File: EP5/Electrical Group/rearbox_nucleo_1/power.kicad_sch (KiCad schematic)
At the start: 10 parts, among them IC1 LMQ66420MC5RXBRQ1, J6 power board

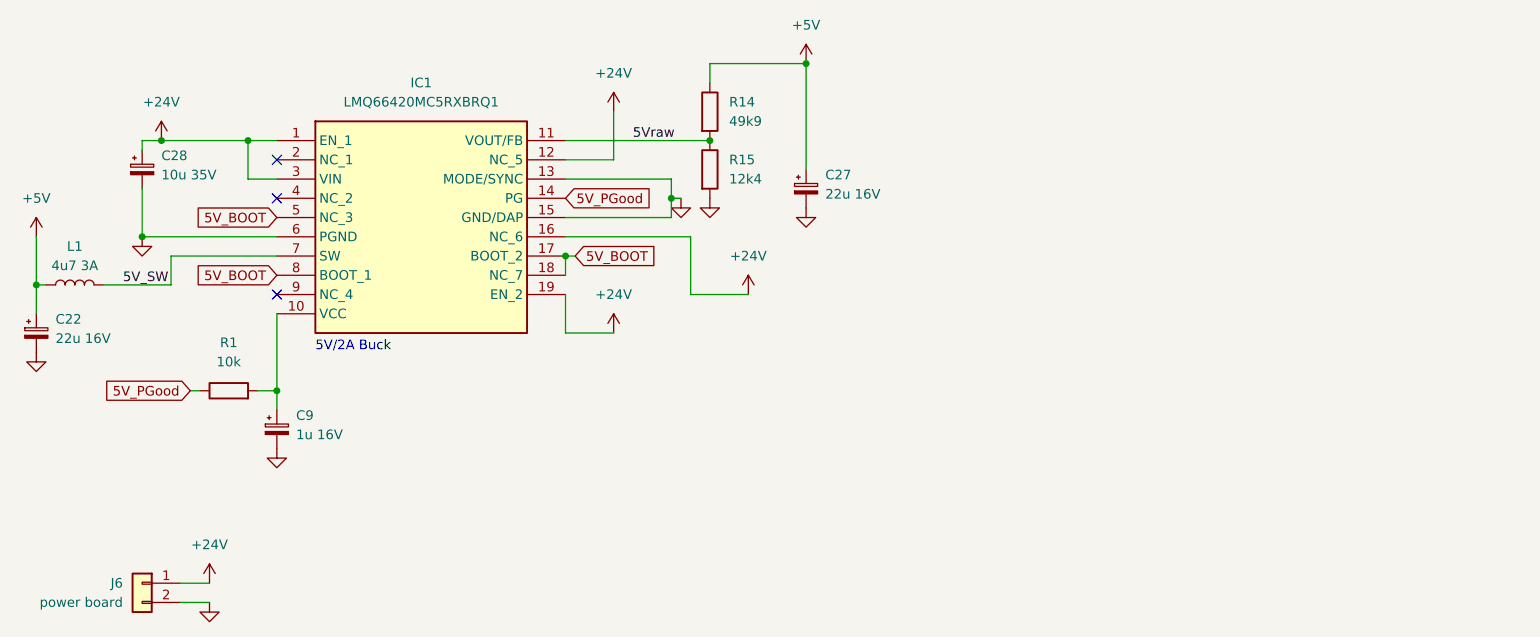
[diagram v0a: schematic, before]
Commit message: update rearbox Nucleo hat to V2.0 to cancel isolation and use IDC socket
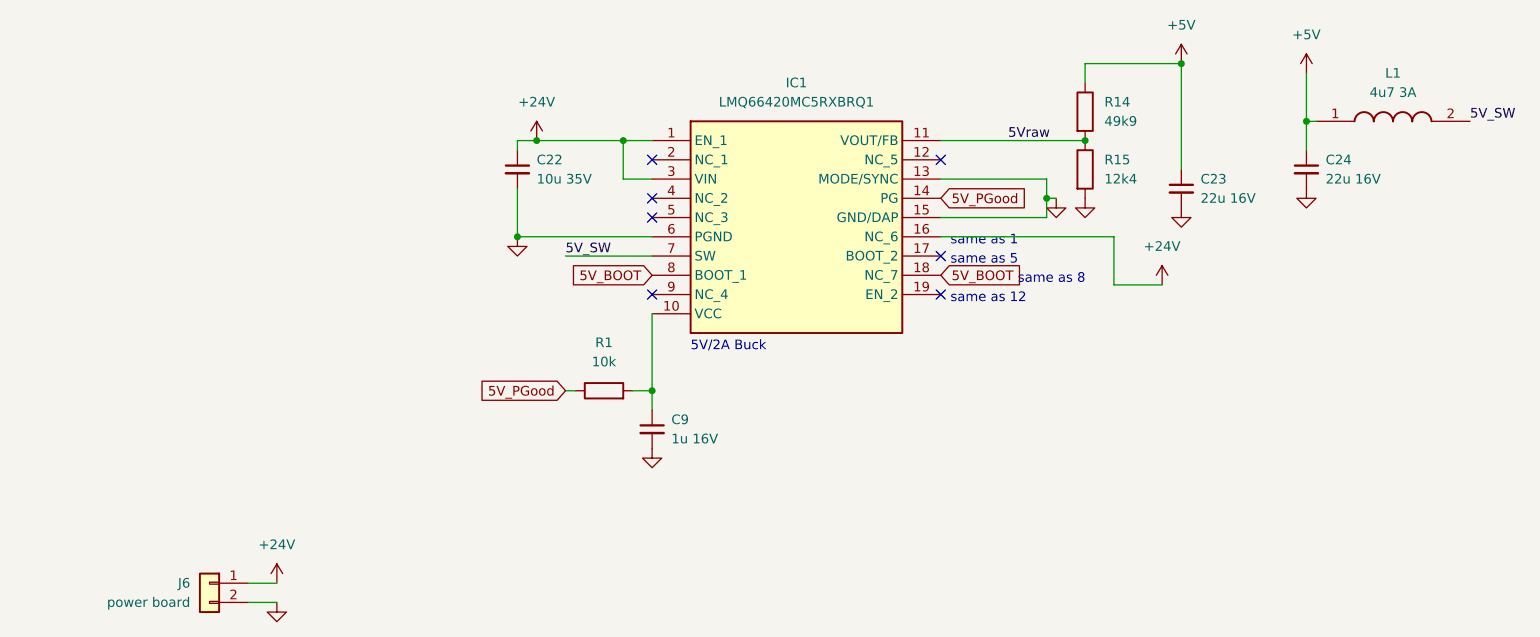
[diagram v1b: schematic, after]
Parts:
- removed C22, C27: 22u 16V, Capacitor_THT:CP_Radial_D5.0mm_P2.50mm, symbol Device:C_Polarized_Small
- removed C28: 10u 35V, Capacitor_THT:CP_Radial_D5.0mm_P2.50mm, symbol Device:C_Polarized_Small
- removed C9: 1u 16V, Capacitor_SMD:C_0805_2012Metric, symbol Device:C_Polarized_Small
- removed L1: 4u7 3A, Inductor_SMD:L_0805_2012Metric, symbol Device:L
- added C22: 10u 35V, Capacitor_SMD:C_1206_3216Metric, symbol Device:C_Small
- added C23, C24: 22u 16V, Capacitor_SMD:C_1206_3216Metric, symbol Device:C_Small
- added C9: 1u 16V, Capacitor_SMD:C_0805_2012Metric, symbol Device:C_Small
- added L1: 4u7 3A, SamacSys_Parts:INDPM5552X300N, symbol SamacSys_Parts:SRP5030WA-2R2M
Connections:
- net +24V: now also C22.1; no longer IC1.12 (NC_5), IC1.19 (EN_2)
- net +5V: now also C23.1, C24.1, L1.1
- net 5V_BOOT: no longer IC1.17 (BOOT_2), IC1.5 (NC_3)
- net 5V_SW: now also L1.2
- net GND: now also C22.2, C23.2, C24.2, C9.2
- net at IC1.10 (VCC), R1.2: now also C9.1
- no-connect marks 3 -> 7
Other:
- note added: "same as 1"
- note added: "same as 12"
- note added: "same as 5"
- note added: "same as 8"
- company: (none) -> NTURacing
- title: (none) -> rear box nucleo board 1
- moved on the sheet: J6, R1, R14, R15

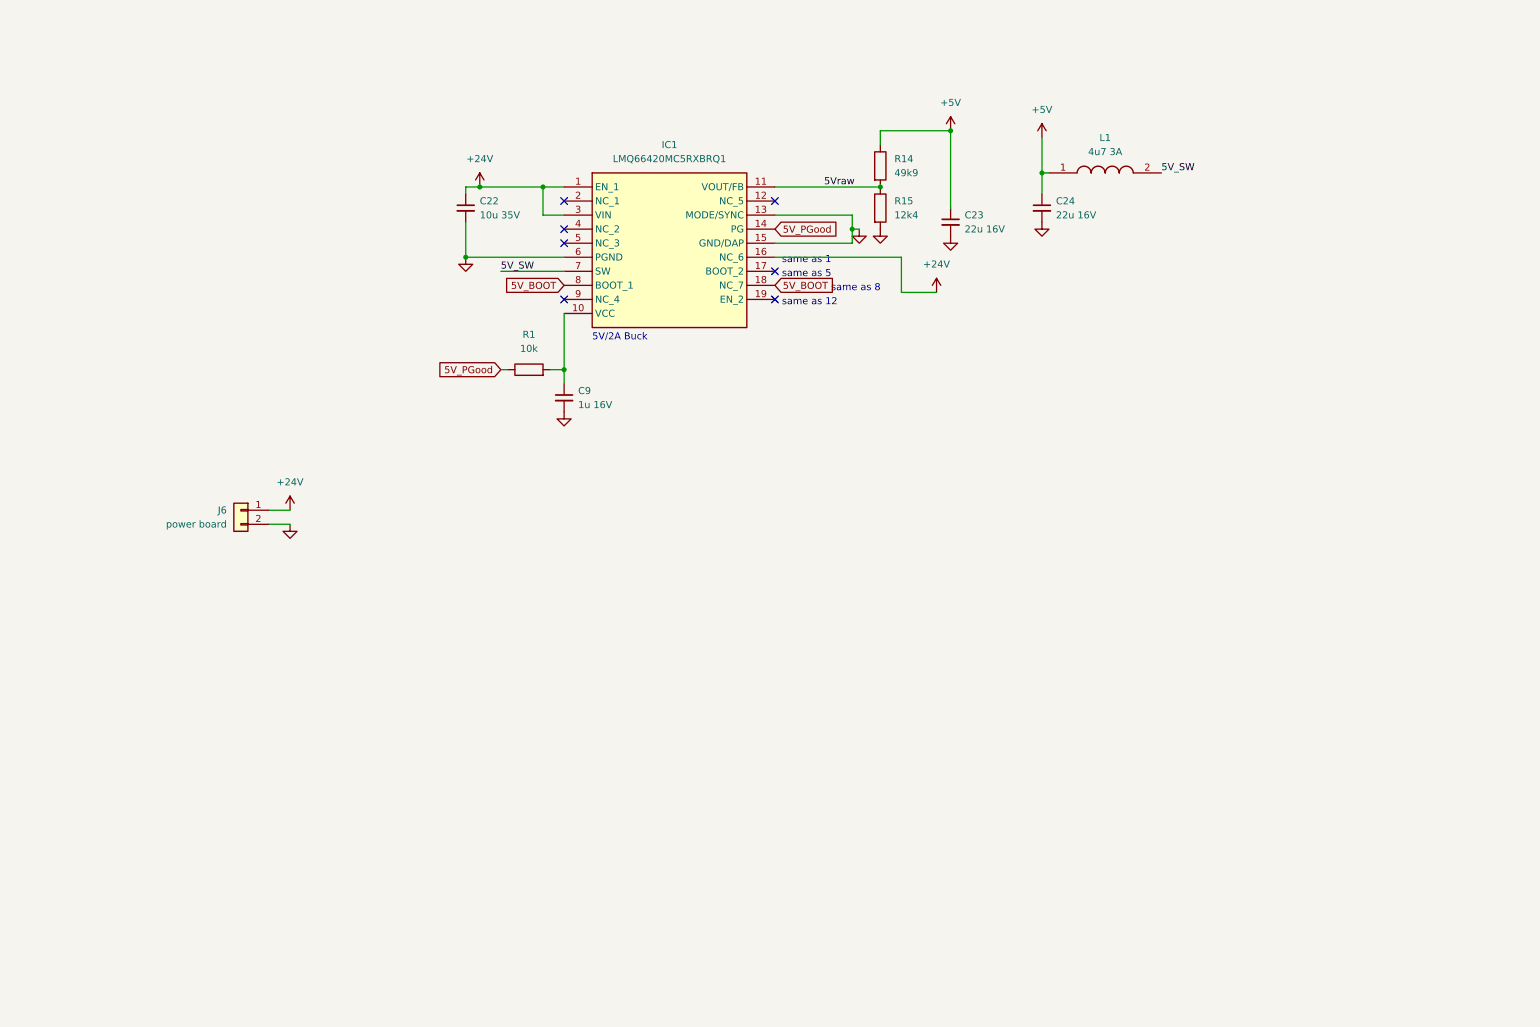
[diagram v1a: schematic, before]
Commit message: update rearbox nucleo hat to V3.0
change buck converter
add fuses and Zener diodes
change CAN transceiver
change power supply of brake light
change MOSFET for buzzer and brake light control
add test pads
add LEDs
fix SD card pin
fix VBAT reveresed
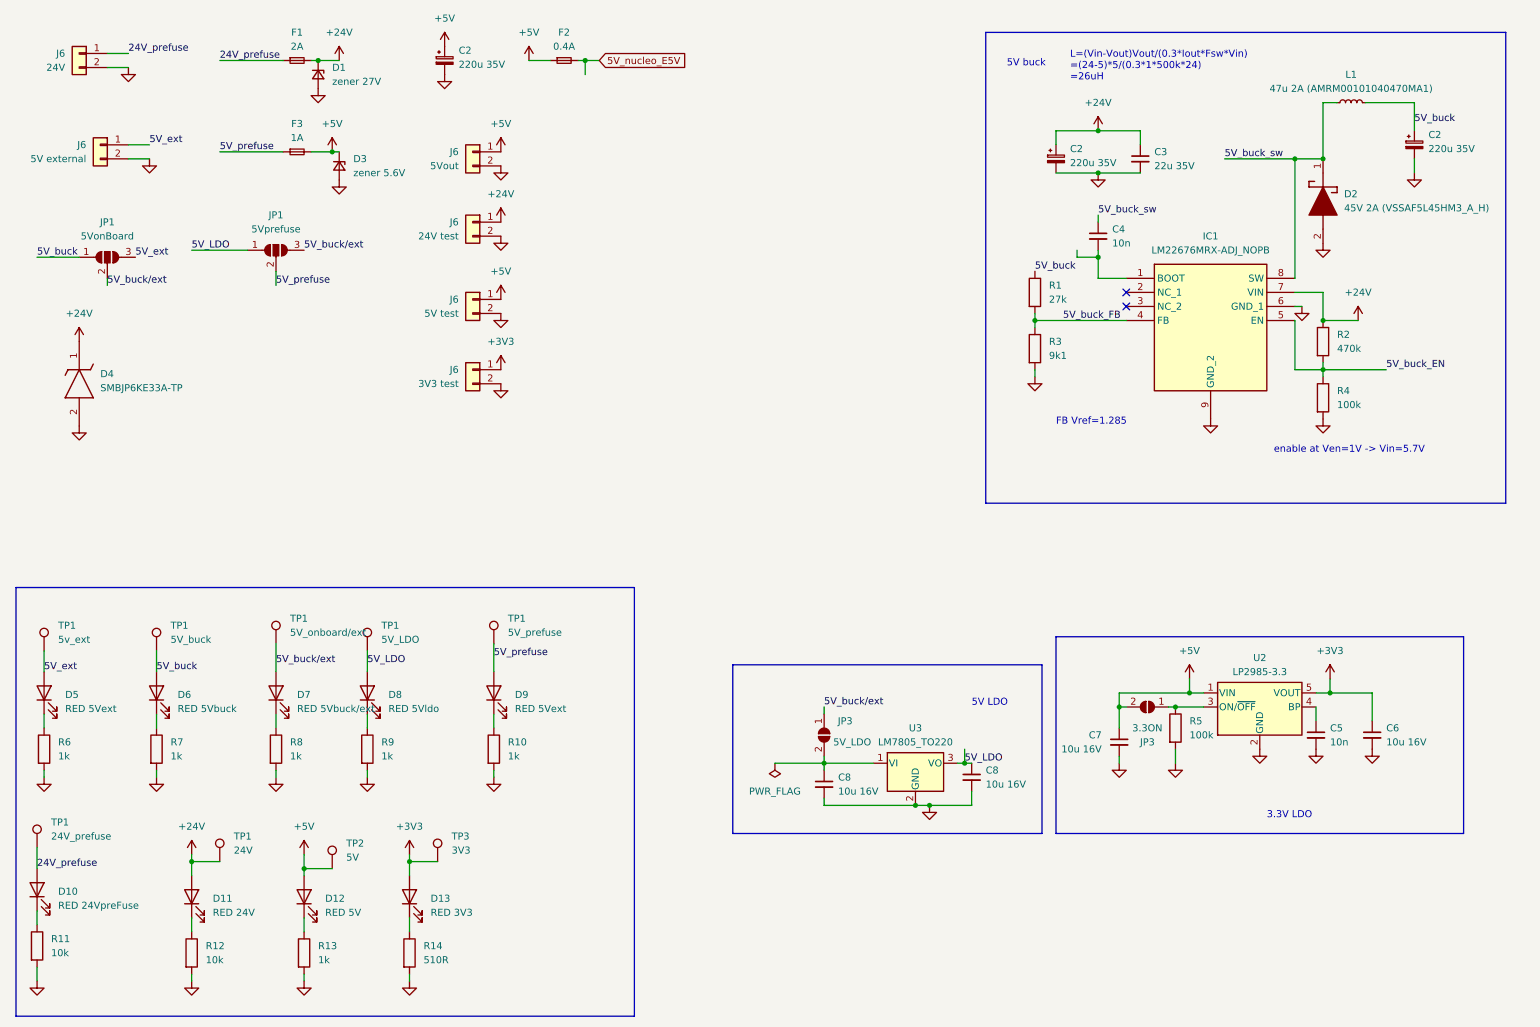
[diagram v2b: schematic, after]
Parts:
- removed C22: 10u 35V, Capacitor_SMD:C_1206_3216Metric, symbol Device:C_Small
- removed C23, C24: 22u 16V, Capacitor_SMD:C_1206_3216Metric, symbol Device:C_Small
- removed C9: 1u 16V, Capacitor_SMD:C_0805_2012Metric, symbol Device:C_Small
- removed IC1: LMQ66420MC5RXBRQ1, SamacSys_Parts:LMR66430R5RXBR, symbol SamacSys_Parts:LMQ66420MC5RXBRQ1
- removed L1: 4u7 3A, SamacSys_Parts:INDPM5552X300N, symbol SamacSys_Parts:SRP5030WA-2R2M
- removed R15: 12k4, Resistor_SMD:R_0603_1608Metric, symbol Device:R
- added C2 (x3): 220u 35V, Capacitor_THT:CP_Radial_D8.0mm_P3.80mm, symbol Device:C_Polarized_Small
- added C3: 22u 35V, Capacitor_SMD:C_1206_3216Metric, symbol Device:C_Small
- added C4, C5: 10n, Capacitor_SMD:C_0603_1608Metric, symbol Device:C_Small
- added C6, C7, C8 (x2): 10u 16V, Capacitor_SMD:C_0805_2012Metric, symbol Device:C_Small
- added D1: zener 27V, Diode_SMD:D_MiniMELF, symbol Device:D_Zener_Small
- added D10: RED 24VpreFuse, LED_SMD:LED_0603_1608Metric, symbol Device:LED
- added D11: RED 24V, LED_SMD:LED_0603_1608Metric, symbol Device:LED
- added D12: RED 5V, LED_SMD:LED_0603_1608Metric, symbol Device:LED
- added D13: RED 3V3, LED_SMD:LED_0603_1608Metric, symbol Device:LED
- added D2: 45V 2A (VSSAF5L45HM3_A_H), SamacSys_Parts:SODFL5226X100N, symbol SamacSys_Parts:VSSAF5L45HM3_A_H
- added D3: zener 5.6V, Diode_SMD:D_MiniMELF, symbol Device:D_Zener_Small
- added D4: SMBJP6KE33A-TP, SamacSys_Parts:DIOM5336X262N, symbol SamacSys_Parts:SMBJP6KE33A-TP
- added D5, D9: RED 5Vext, LED_SMD:LED_0603_1608Metric, symbol Device:LED
- added D6: RED 5Vbuck, LED_SMD:LED_0603_1608Metric, symbol Device:LED
- added D7: RED 5Vbuck/ext, LED_SMD:LED_0603_1608Metric, symbol Device:LED
- added D8: RED 5Vldo, LED_SMD:LED_0603_1608Metric, symbol Device:LED
- added F1: 2A, Fuse:Fuse_2512_6332Metric_Pad1.52x3.35mm_HandSolder, symbol Device:Fuse_Small
- added F2: 0.4A, Fuse:Fuse_2512_6332Metric_Pad1.52x3.35mm_HandSolder, symbol Device:Fuse_Small
- added F3: 1A, Fuse:Fuse_2512_6332Metric_Pad1.52x3.35mm_HandSolder, symbol Device:Fuse_Small
- added IC1: LM22676MRX-ADJ_NOPB, SamacSys_Parts:SOIC127P600X170-9N, symbol SamacSys_Parts:LM22676MRX-ADJ_NOPB
- added J6: 24V test, Connector_PinHeader_2.54mm:PinHeader_1x02_P2.54mm_Vertical, symbol Connector_Generic:Conn_01x02
- added J6: 5V test, Connector_PinHeader_2.54mm:PinHeader_1x02_P2.54mm_Vertical, symbol Connector_Generic:Conn_01x02
- added J6: 5V external, Connector_JST:JST_XH_B2B-XH-A_1x02_P2.50mm_Vertical, symbol Connector_Generic:Conn_01x02
- added J6: 3V3 test, Connector_PinHeader_2.54mm:PinHeader_1x02_P2.54mm_Vertical, symbol Connector_Generic:Conn_01x02
- added J6: 5Vout, Connector_JST:JST_XH_B2B-XH-A_1x02_P2.50mm_Vertical, symbol Connector_Generic:Conn_01x02
- added JP1: 5VonBoard, Jumper:SolderJumper-3_P1.3mm_Open_Pad1.0x1.5mm_NumberLabels, symbol Jumper:SolderJumper_3_Open
- added JP1: 5Vprefuse, Jumper:SolderJumper-3_P1.3mm_Open_Pad1.0x1.5mm_NumberLabels, symbol Jumper:SolderJumper_3_Open
- added JP3: 3.3ON, Jumper:SolderJumper-2_P1.3mm_Open_Pad1.0x1.5mm, symbol Jumper:SolderJumper_2_Open
- added JP3: 5V_LDO, Jumper:SolderJumper-2_P1.3mm_Open_Pad1.0x1.5mm, symbol Jumper:SolderJumper_2_Open
- added L1: 47u 2A (AMRM00101040470MA1), SamacSys_Parts:AMRM00101040470MA1, symbol Device:L_Small
- added R10, R13, R6, R7, R8, R9: 1k, Resistor_SMD:R_0603_1608Metric, symbol Device:R
- added R11, R12: 10k, Resistor_SMD:R_0603_1608Metric, symbol Device:R
- added R2: 470k, Resistor_SMD:R_0603_1608Metric, symbol Device:R
- added R3: 9k1, Resistor_SMD:R_0603_1608Metric, symbol Device:R
- added R4, R5: 100k, Resistor_SMD:R_0603_1608Metric, symbol Device:R
- added TP1: 24V, TestPoint:TestPoint_Pad_D1.0mm, symbol Connector:TestPoint
- added TP1: 24V_prefuse, TestPoint:TestPoint_Pad_D1.0mm, symbol Connector:TestPoint
- added TP1: 5V_buck, TestPoint:TestPoint_Pad_D1.0mm, symbol Connector:TestPoint
- added TP1: 5V_prefuse, TestPoint:TestPoint_Pad_D1.0mm, symbol Connector:TestPoint
- added TP1: 5v_ext, TestPoint:TestPoint_Pad_D1.0mm, symbol Connector:TestPoint
- added TP1: 5V_LDO, TestPoint:TestPoint_Pad_D1.0mm, symbol Connector:TestPoint
- added TP1: 5V_onboard/ext, TestPoint:TestPoint_Pad_D1.0mm, symbol Connector:TestPoint
- added TP2: 5V, TestPoint:TestPoint_Pad_D1.0mm, symbol Connector:TestPoint
- added TP3: 3V3, TestPoint:TestPoint_Pad_D1.0mm, symbol Connector:TestPoint
- added U2: LP2985-3.3, Package_TO_SOT_SMD:SOT-23-5, symbol Regulator_Linear:LP2985-3.3
- added U3: LM7805_TO220, Package_TO_SOT_THT:TO-220-3_Vertical, symbol Regulator_Linear:LM7805_TO220
- J6: value power board -> 24V
- R1: value 10k -> 27k
- R14: value 49k9 -> 510R
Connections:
- net 5Vraw is gone; now on net GND: R14.2
- net +24V: now also C2.1, C3.1, D1.1 (K), D11.2 (A), D4.1 (K), F1.2, IC1.7 (VIN), J6.1 (Pin_1), R2.1, TP1.1; no longer J6.1 (Pin_1)
- net +5V: now also C2.1, C7.1, D12.2 (A), D3.1 (K), F2.1, F3.2, J6.1 (Pin_1), J6.1 (Pin_1), JP3.2 (B), TP2.1, U2.1 (VIN); no longer R14.1
- net GND: now also C2.2, C2.2, C2.2, C3.2, C5.2, C6.2, C7.2, C8.2, C8.2, D1.2 (A), D2.2 (A), D3.2 (A), D4.2 (A), IC1.6 (GND_1), IC1.9 (GND_2), J6.2 (Pin_2), J6.2 (Pin_2), J6.2 (Pin_2), J6.2 (Pin_2), J6.2 (Pin_2), R10.2, R11.2, R12.2, R13.2, R3.2, R4.2, R5.2, R6.2, R7.2, R8.2, R9.2, U2.2 (GND), U3.2 (GND)
- net 5V_buck_FB: now reaches R1.2
- net 5V_buck_FB: now also IC1.4 (FB), R3.1
- net 5V_PGood renamed 5V_buck
- net 5V_buck: now also C2.1, D6.2 (A), JP1.1 (A), L1.2, TP1.1
- new net: D12.1 (K), R13.1
- new net: C8.1, JP3.2 (B), U3.1 (VI)
- new net: D11.1 (K), R12.1
- new net: C4.2, IC1.1 (BOOT)
- new net: D10.1 (K), R11.1
- new net: D5.1 (K), R6.1
- new net: D6.1 (K), R7.1
- new net: D13.1 (K), R14.1
- new net: JP3.1 (A), R5.1, U2.3 (ON/~{OFF})
- new net: D7.1 (K), R8.1
- new net: C5.1, U2.4 (BP)
- new net: D9.1 (K), R10.1
- new net: D8.1 (K), R9.1
- new net +3V3: C6.1, D13.2 (A), J6.1 (Pin_1), TP3.1, U2.5 (VOUT)
- new net 24V_prefuse: D10.2 (A), F1.1, J6.1 (Pin_1), TP1.1
- new net 5V_LDO: C8.1, D8.2 (A), JP1.1 (A), TP1.1, U3.3 (VO)
- new net 5V_buck_EN: IC1.5 (EN), R2.2, R4.1
- new net 5V_buck_sw: C4.1, D2.1 (K), IC1.8 (SW), L1.1
- new net 5V_buck/ext: D7.2 (A), JP1.2 (C), JP1.3 (B), JP3.1 (A), TP1.1
- new net 5V_ext: D5.2 (A), J6.1 (Pin_1), JP1.3 (B), TP1.1
- new net 5V_nucleo_E5V: F2.2
- new net 5V_prefuse: D9.2 (A), F3.1, JP1.2 (C), TP1.1
- no-connect marks 7 -> 2
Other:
- note added: "3.3V LDO"
- note added: "5V LDO"
- note added: "5V buck"
- note added: "FB Vref=1.285"
- note added: "L=(Vin-Vout)Vout/(0.3*Iout*Fsw*Vin) =(24-5)*5/(0.3*1*500k*24) =26uH"
- note added: "enable at Ven=1V -> Vin=5.7V"
- note removed: "5V/2A Buck"
- note removed: "same as 1"
- note removed: "same as 12"
- note removed: "same as 5"
- note removed: "same as 8"
- moved on the sheet: J6

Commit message: update rearbox nucleo hat to V3.1
use buck converter as current source and rather than voltage source
add 24v voltage and current measurement
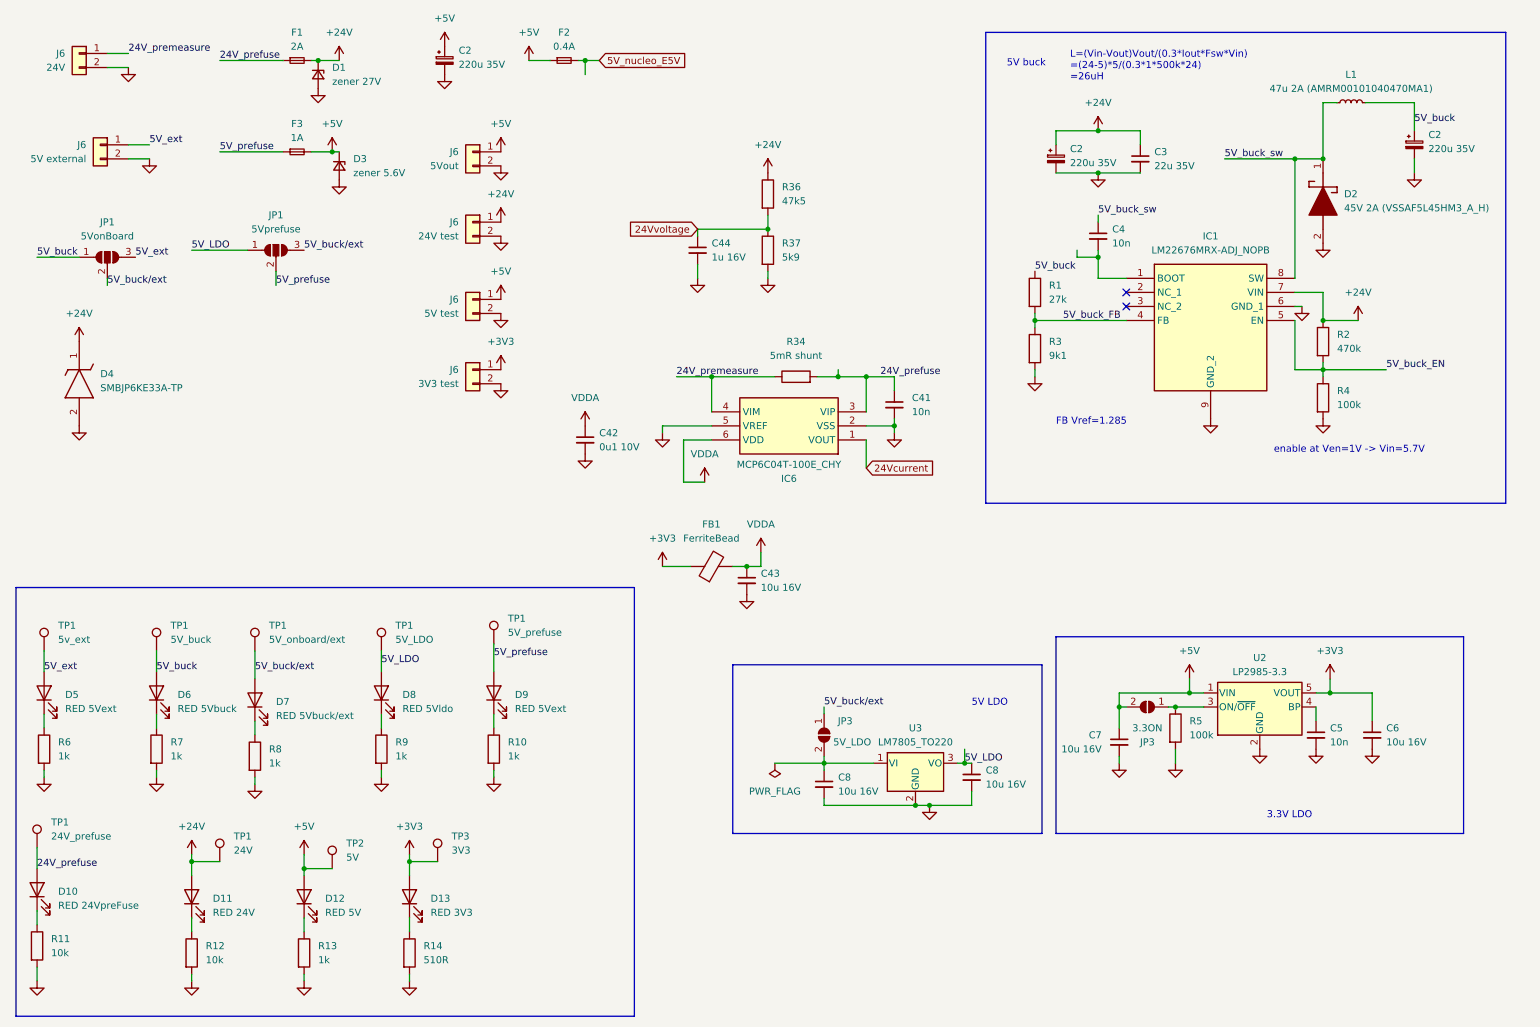
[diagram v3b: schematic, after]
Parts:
- added C41: 10n, Capacitor_SMD:C_0805_2012Metric, symbol Device:C_Small
- added C42: 0u1 10V, Capacitor_SMD:C_0805_2012Metric, symbol Device:C_Small
- added C43: 10u 16V, Capacitor_SMD:C_0805_2012Metric, symbol Device:C_Small
- added C44: 1u 16V, Capacitor_SMD:C_0805_2012Metric, symbol Device:C_Small
- added FB1: FerriteBead, Inductor_SMD:L_0805_2012Metric, symbol Device:FerriteBead
- added IC6: MCP6C04T-100E_CHY, SamacSys_Parts:SOT95P280X145-6N, symbol SamacSys_Parts:MCP6C04T-100E_CHY
- added R34: 5mR shunt, Resistor_SMD:R_1206_3216Metric, symbol Device:R
- added R36: 47k5, Resistor_SMD:R_0603_1608Metric, symbol Device:R
- added R37: 5k9, Resistor_SMD:R_0603_1608Metric, symbol Device:R
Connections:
- net +24V: now also R36.1
- net +3V3: now also FB1.1
- net 24V_prefuse: now also C41.1, IC6.3 (VIP), R34.2; no longer J6.1 (Pin_1)
- net GND: now also C41.2, C42.2, C43.2, C44.2, IC6.2 (VSS), IC6.5 (VREF), R37.2
- new net 24V_premeasure: IC6.4 (VIM), J6.1 (Pin_1), R34.1
- new net 24Vcurrent: IC6.1 (VOUT)
- new net 24Vvoltage: C44.1, R36.2, R37.1
- new net VDDA: C42.1, C43.1, FB1.2, IC6.6 (VDD)
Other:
- moved on the sheet: D7, D8, R8, R9, TP1
